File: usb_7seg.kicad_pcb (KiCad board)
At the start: 2 copper layers, 72 x 47 mm, 8 parts, among them IC1 MAX7219CNG, IC2 MAX7219CWG, U1 SeeeduinoXIAO, U2 7segment_led

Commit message: とりあえず完成。DRCもok
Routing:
- net Net-(IC1-Pad16): track 6.62 -> 89.3 mm, vias 0 -> 1
- net Net-(IC1-Pad15): track 7.89 -> 81.2 mm, vias 0 -> 1
- net Net-(IC1-Pad14): track 9.49 -> 78.0 mm, vias 0 -> 1
- net Net-(IC1-Pad21): track 5.76 -> 64.4 mm, vias 0 -> 1
- net Net-(IC1-Pad12): track 11.0 -> 64.4 mm, vias 0 -> 2
- net +5V: track 4.98 -> 57.6 mm
- net Net-(IC1-Pad17): track 5.65 -> 57.4 mm
- net GND: track 27.7 -> 77.0 mm
- net Net-(IC1-Pad23): track 7.46 -> 56.4 mm
- net Net-(IC1-Pad20): track 4.60 -> 52.8 mm
- net Net-(IC1-Pad22): track 6.29 -> 53.8 mm
- net Net-(IC1-Pad13): track 10.1 -> 56.9 mm, vias 0 -> 1
- net Net-(IC1-Pad11): track 10.4 -> 55.9 mm
- net Net-(IC1-Pad6): track 6.09 -> 42.0 mm
- net Net-(IC1-Pad7): track 6.61 -> 30.8 mm, vias 0 -> 1
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
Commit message: ベタグラ書け忘れてた
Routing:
- added copper zone on B.Cu, net GND
- added copper zone on F.Cu, net GND
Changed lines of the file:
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@@
   (page A4)
   (layers
-    (0 F.Cu signal)
+    (0 F.Cu signal hide)
     (31 B.Cu signal)
     (32 B.Adhes user)
@@
   (segment (start 21.59 44.45) (end 20.32 43.18) (width 0.25) (layer F.Cu) (net 39))
   (segment (start 20.32 39.53) (end 20.32 43.18) (width 0.25) (layer F.Cu) (net 39))
+  (zone (net 1) (net_name GND) (layer F.Cu) (hatch edge 0.508)
+    (connect_pads (clearance 0.508))
+    (min_thickness 0.254)
+    (fill yes (arc_segments 32) (thermal_gap 0.508) (thermal_bridge_width 0.508))
+    (polygon
+      (pts
+        (xy 74.93 -2.54) (xy 74.93 49.53) (xy -2.54 49.53) (xy -2.54 -2.54)
+      )
+    )
+  )
+  (zone (net 1) (net_name GND) (layer B.Cu) (hatch edge 0.508)
+    (connect_pads (clearance 0.508))
+    (min_thickness 0.254)
+    (fill yes (arc_segments 32) (thermal_gap 0.508) (thermal_bridge_width 0.508))
+    (polygon
+      (pts
+        (xy 74.93 -2.54) (xy 74.93 49.53) (xy -2.54 49.53) (xy -2.54 -2.54)
+      )
+    )
+  )
 )

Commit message: いろいろ修正した
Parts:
- C1  10uF: renamed from C1
- R1   10k: renamed from R1
- U1: footprint Seeeduino XIAO:Seeeduino XIAO-MOUDLE14P-2.54-21X17.8MM -> kicad_mylib:SeeedXIAO
- U2: footprint kicad_7segment_led:kicad_7segment_led_0.56 -> kicad_mylib:7segment_led_0.56
- moved U1 47.8 mm to (40.9, -24.1)
- moved C1  10uF 47.0 mm to (34.3, -2.54)
- moved IC1 47.0 mm to (21.6, -11.4)
- moved IC2 47.0 mm to (22.9, -16.5)
- moved R1   10k 47.0 mm to (19.1, -2.54)
- moved ~ 47.0 mm to (36.8, -2.54)
- moved ~ 47.0 mm to (24.1, -2.54)
- moved U2 47.0 mm to (11.0, -25.4)
- renumbered C2 to ~, R2 to ~
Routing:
- net GND: track 77.0 -> 0.00 mm
- net Net-(IC1-Pad12): track 64.4 -> 50.0 mm
- net Net-(IC1-Pad1): track 32.0 -> 20.3 mm
- net Net-(IC1-Pad13): track 56.9 -> 48.2 mm, vias 1 -> 0
- net +5V: track 57.6 -> 49.0 mm
- net Net-(IC1-Pad17): track 57.4 -> 49.8 mm
- net Net-(IC1-Pad20): track 52.8 -> 45.3 mm
- net Net-(IC1-Pad22): track 53.8 -> 46.5 mm
- net Net-(IC1-Pad23): track 56.4 -> 50.9 mm
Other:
- outline, holes or cut-outs redrawn
- board text added: "2020 REALGLOBE Inc rev 0.2"
- board text removed: "2020 REALGLOBE Inc rev 0.1"

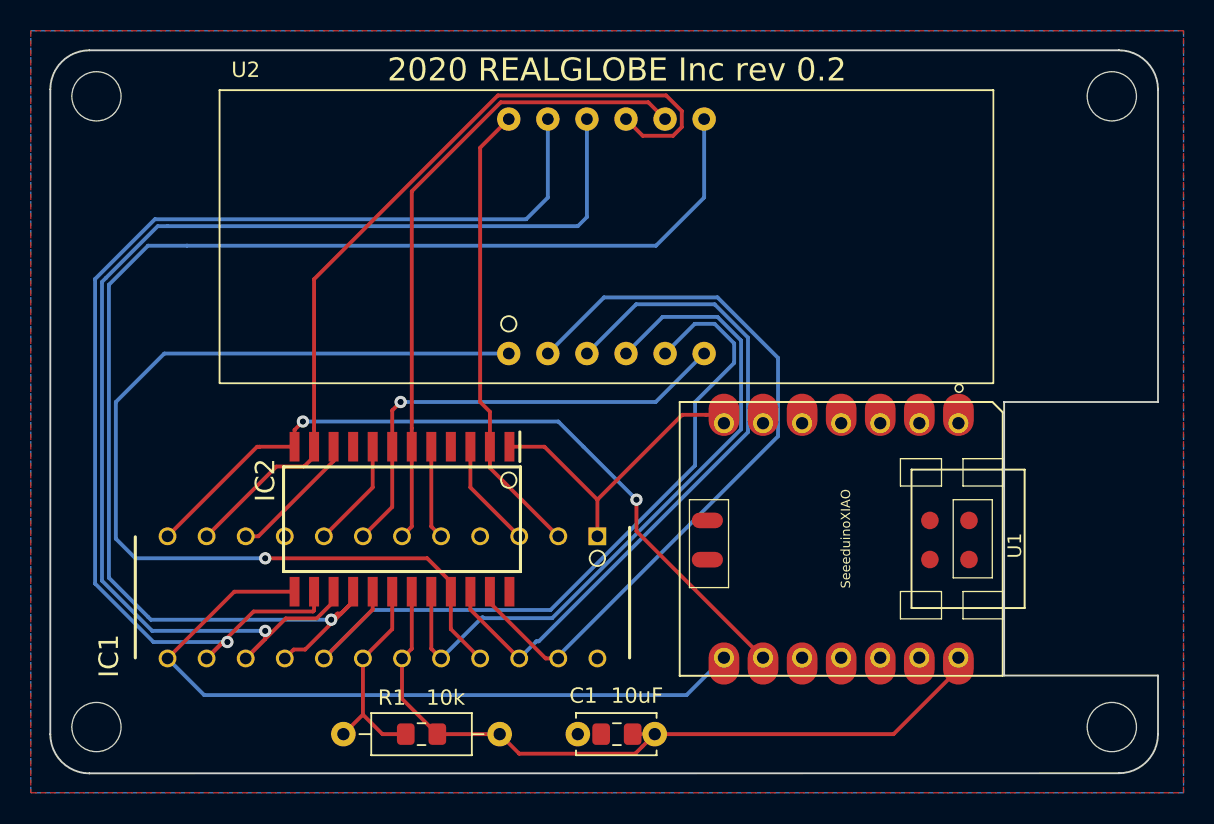
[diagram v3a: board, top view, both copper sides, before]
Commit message: 配線を消して、部品を仮置きした
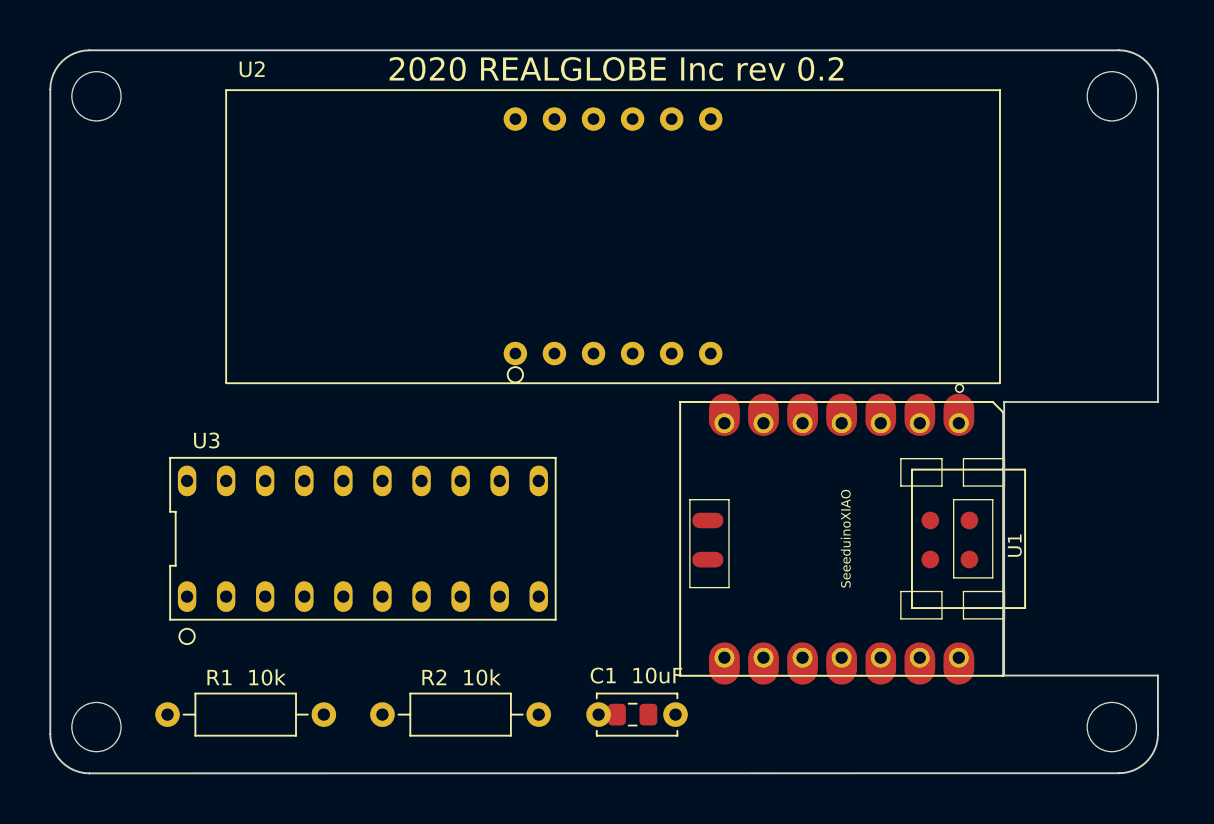
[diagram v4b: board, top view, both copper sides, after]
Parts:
- removed IC1: MAX7219CNG, MAX7219CNG:MAX7219CNG
- removed IC2: MAX7219CWG, MAX7219CWG:MAX7219CWG
- removed R1   10k: R, Resistor_THT:R_Axial_DIN0207_L6.3mm_D2.5mm_P10.16mm_Horizontal
- removed the ~ at (24.1, -2.54)
- added R1  10k: 10k, Resistor_THT:R_Axial_DIN0207_L6.3mm_D2.5mm_P10.16mm_Horizontal, F.Cu at (7.62, -3.81)
- added R2  10k: 10k, Resistor_THT:R_Axial_DIN0207_L6.3mm_D2.5mm_P10.16mm_Horizontal, F.Cu at (21.6, -3.81)
- added U3: TM1637, kicad_mylib:TM1630, F.Cu at (7.62, -10.2)
- C1  10uF: value C -> 10uF
- ~: value C -> 10uF
- moved C1  10uF 1.85 mm to (35.6, -3.81)
- moved ~ 1.63 mm to (37.9, -3.81)
- moved U2 0.43 mm to (11.4, -25.4)
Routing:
- net Net-(U2-Pad7): track 89.3 -> 0.00 mm, vias 1 -> 0
- net Net-(U2-Pad10): track 81.2 -> 0.00 mm, vias 1 -> 0
- net Net-(U2-Pad11): track 78.0 -> 0.00 mm, vias 1 -> 0
- net Net-(U2-Pad1): track 64.4 -> 0.00 mm, vias 1 -> 0
- net Net-(U2-Pad9): track 55.9 -> 0.00 mm
- net Net-(U2-Pad2): track 50.9 -> 0.00 mm
- net Net-(R1-Pad2): track 50.0 -> 0.00 mm, vias 2 -> 0
- net Net-(U2-Pad5): track 49.8 -> 0.00 mm
- net +5V: track 49.0 -> 0.00 mm
- net Net-(R2-Pad2): track 48.2 -> 0.00 mm
- net Net-(U2-Pad3): track 46.5 -> 0.00 mm
- net Net-(U2-Pad4): track 45.3 -> 0.00 mm
- net Net-(U2-Pad8): track 42.0 -> 0.00 mm
- net Net-(U2-Pad12): track 31.5 -> 0.00 mm
- net Net-(U2-Pad6): track 30.8 -> 0.00 mm, vias 1 -> 0
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- removed copper zone on B.Cu, net GND
- removed copper zone on F.Cu, net GND

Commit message: とりあえず配線完了 DRC ok
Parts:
- removed C1  10uF: 10uF, Capacitor_THT:C_Disc_D5.0mm_W2.5mm_P5.00mm
- removed U3: TM1637, kicad_mylib:TM1630
- added C1  100uF: 10uF, Capacitor_THT:C_Disc_D5.0mm_W2.5mm_P5.00mm, F.Cu at (34.3, -5.08)
- added U3  TM1637: TM1637, kicad_mylib:TM1630, F.Cu at (10.2, -11.4)
- added ~: akizuki_C_plate_lower_right, kicad_mylib:akizuki_C_plate_lower_right, F.Cu at (0.00, 0.00)
- moved R1  10k 1.80 mm to (6.35, -5.08)
- moved R2  10k 1.80 mm to (20.3, -5.08)
- moved ~ 1.50 mm to (36.8, -4.85)
- moved U1 0.30 mm to (40.6, -24.1)
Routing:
- net +5V: track 0.00 -> 79.0 mm
- net Net-(R2-Pad2): track 0.00 -> 59.9 mm
- net Net-(R1-Pad2): track 0.00 -> 51.2 mm
- net Net-(U2-Pad7): track 0.00 -> 50.6 mm
- net Net-(U2-Pad11): track 0.00 -> 40.9 mm
- net Net-(U2-Pad10): track 0.00 -> 34.7 mm
- net Net-(U2-Pad4): track 0.00 -> 30.1 mm
- net Net-(U2-Pad8): track 0.00 -> 26.9 mm
- net Net-(U2-Pad9): track 0.00 -> 26.9 mm
- net Net-(U2-Pad5): track 0.00 -> 26.8 mm
- net Net-(U2-Pad12): track 0.00 -> 24.8 mm
- net Net-(U2-Pad2): track 0.00 -> 23.2 mm
- net Net-(U2-Pad3): track 0.00 -> 18.5 mm
- net Net-(U2-Pad1): track 0.00 -> 17.8 mm
- net Net-(U2-Pad6): track 0.00 -> 15.8 mm
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- added copper zone on B.Cu, net GND
- added copper zone on F.Cu, net GND
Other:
- board size 72 x 47 mm -> 72 x 47.5 mm
- board text added: "2020 REALGLOBE Inc rev 0.3"
- board text removed: "2020 REALGLOBE Inc rev 0.2"
